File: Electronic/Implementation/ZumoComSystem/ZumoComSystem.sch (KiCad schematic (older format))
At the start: 0 parts

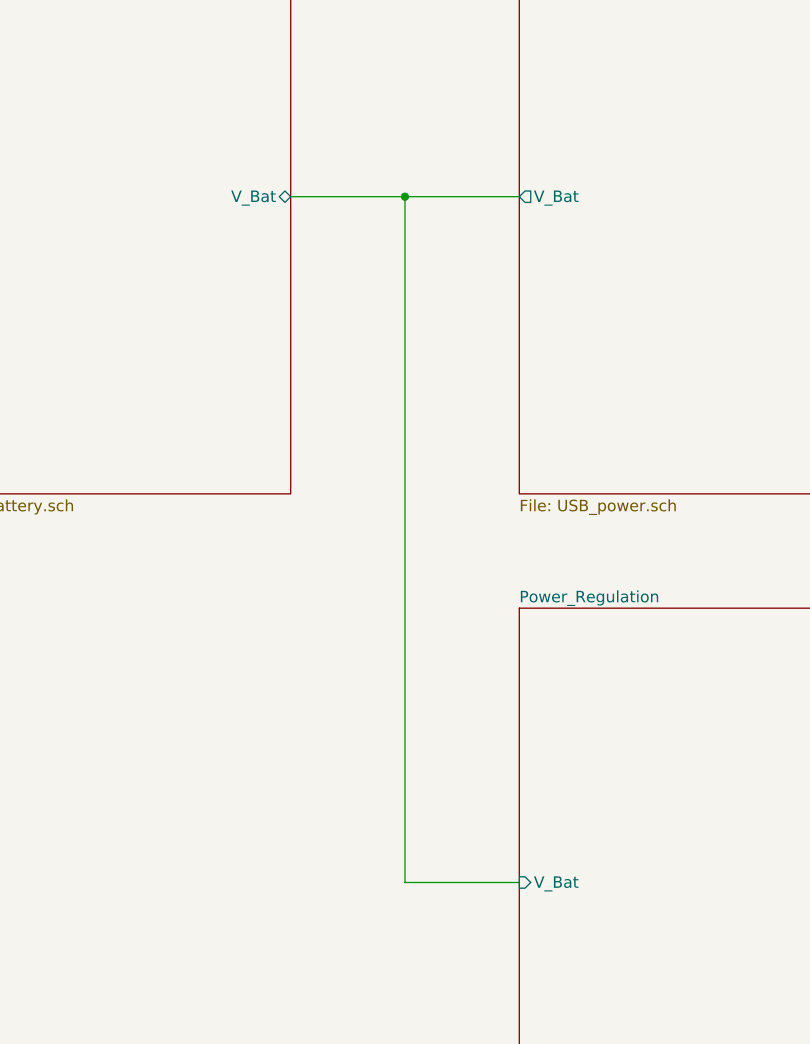
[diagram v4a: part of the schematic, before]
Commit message: electronic: BOM: n-mosfet; SMD-pin correct position
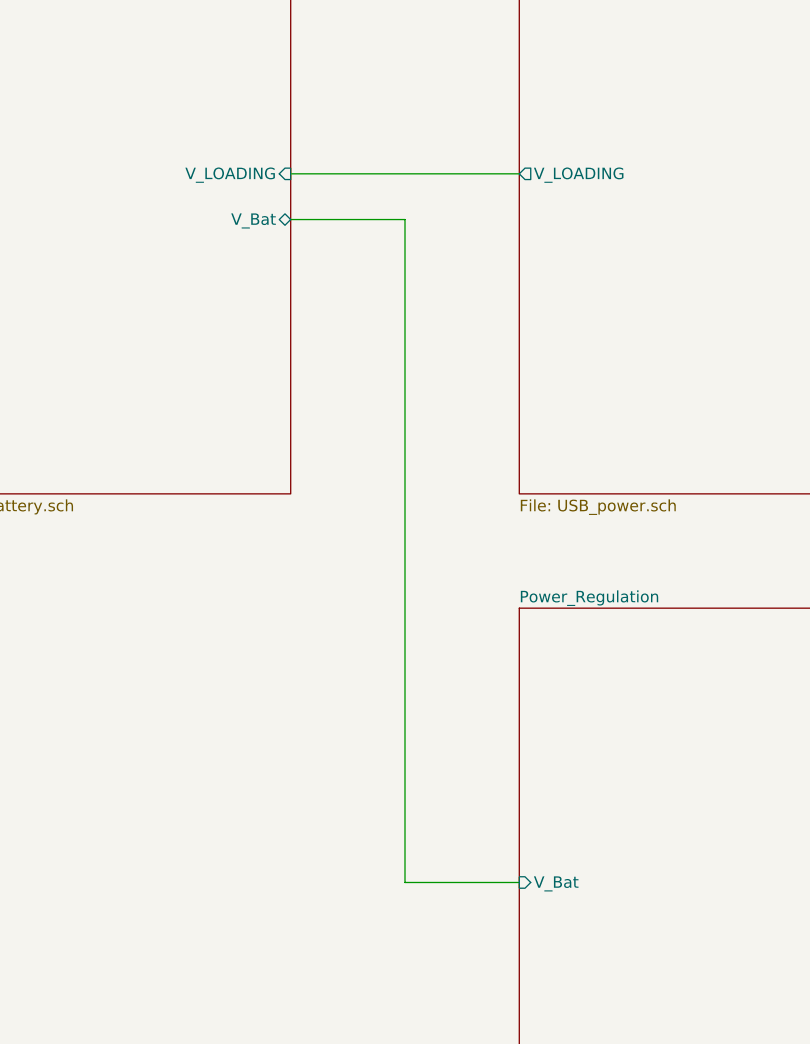
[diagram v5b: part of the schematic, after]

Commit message: Electronic: no charger, added Cp2102 instead of Ft232, first palcement
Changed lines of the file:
@@
 Sheet 1 7
 Title "Zumo Communication System"
-Date "2021-08-20"
+Date "2022-03-08"
 Rev "V1.0"
 Comp "NewTec GmbH"
@@
 Wire Wire Line
 	3500 5000 4000 5000
-Wire Bus Line
-	5500 1900 6500 1900
-Wire Bus Line
-	5500 2100 6500 2100
 Wire Wire Line
 	6500 2500 5800 2500
@@
 F7 "D+" B L 6500 1900 50
 F8 "D-" B L 6500 2100 50
-F9 "nBUTTON_A" I R 8000 1450 50
-F10 "nBUTTON_B" I R 8000 1550 50
-F11 "nBUTTON_C" I R 8000 1650 50
-F12 "nLED_A" O R 8000 1900 50
-F13 "nLED_B" O R 8000 2000 50
-F14 "nLED_C" O R 8000 2100 50
-F15 "nRGB_LED_R" O R 8000 2650 50
-F16 "nRGB_LED_G" O R 8000 2750 50
-F17 "nRGB_LED_B" O R 8000 2850 50
-F18 "nRST" O R 8000 2400 50
-F19 "nRemote_Butt_A" O R 8000 1000 50
-F20 "nRemote_Butt_B" O R 8000 1100 50
-F21 "nRemote_Butt_C" O R 8000 1200 50
-F22 "nON_OFF" O R 8000 3050 50
+F9 "nLED_A" O R 8000 1900 50
+F10 "nLED_B" O R 8000 2000 50
+F11 "nLED_C" O R 8000 2100 50
+F12 "nRGB_LED_R" O R 8000 2650 50
+F13 "nRGB_LED_G" O R 8000 2750 50
+F14 "nRGB_LED_B" O R 8000 2850 50
+F15 "nRST" O R 8000 2400 50
+F16 "nON_OFF" O R 8000 3050 50
+F17 "nBUT_B" I R 8000 1550 50
+F18 "nBUT_C" I R 8000 1650 50
+F19 "nBUT_A" I R 8000 1450 50
 $EndSheet
-Wire Wire Line
-	9500 1000 8000 1000
-Wire Wire Line
-	8000 1100 9500 1100
-Wire Wire Line
-	9500 1200 8000 1200
 Wire Wire Line
 	9500 3050 8000 3050
@@
 F3 "nLED_C" I L 9500 2100 50
 F4 "nLED_A" I L 9500 1900 50
-F5 "nBUTTON_B" O L 9500 1550 50
-F6 "nBUTTON_C" O L 9500 1650 50
-F7 "nBUTTON_A" O L 9500 1450 50
-F8 "nRGB_LED_R" I L 9500 2650 50
-F9 "nRGB_LED_G" I L 9500 2750 50
-F10 "nRGB_LED_B" I L 9500 2850 50
-F11 "nRemote_Butt_A" I L 9500 1000 50
-F12 "nRemote_Butt_B" I L 9500 1100 50
-F13 "nRemote_Butt_C" I L 9500 1200 50
-F14 "nRST" I L 9500 2400 50
-F15 "nON_OFF" I L 9500 3050 50
+F5 "nRGB_LED_R" I L 9500 2650 50
+F6 "nRGB_LED_G" I L 9500 2750 50
+F7 "nRGB_LED_B" I L 9500 2850 50
+F8 "nRST" I L 9500 2400 50
+F9 "nON_OFF" I L 9500 3050 50
+F10 "nBUT_C" O L 9500 1650 50
+F11 "nBUT_B" O L 9500 1550 50
+F12 "nBUT_A" O L 9500 1450 50
 $EndSheet
+Wire Wire Line
+	5500 1900 6500 1900
+Wire Wire Line
+	5500 2100 6500 2100
 $EndSCHEMATC
